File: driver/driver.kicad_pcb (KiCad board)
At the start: 2 copper layers, 131.4 x 100 mm, 99 parts, among them J1 OUT_A, J10 FAN, J2 OUT_B, J4 RJ45_LED_Shielded, J5 RJ45_LED_Shielded, J6 1602 I2C LCD, J7 IN_VCC, J8 IN_GND, J9 SWD, Q1 TPHR6503PL, Q2 TPHR6503PL, Q3 TPHR6503PL, Q4 TPHR6503PL, U1 MT3608, U10 PC817, U11 AMS1117-5.0, U12 PC817, U13 MAX485E, U2 74HC595, U3 AMS1117-3.3, U4 TC4427, U5 TC4427, U6 STM32F030F4Px, U7 INA226, U8 MCP9804_MSOP, U9 PC817, Y1 8MHz

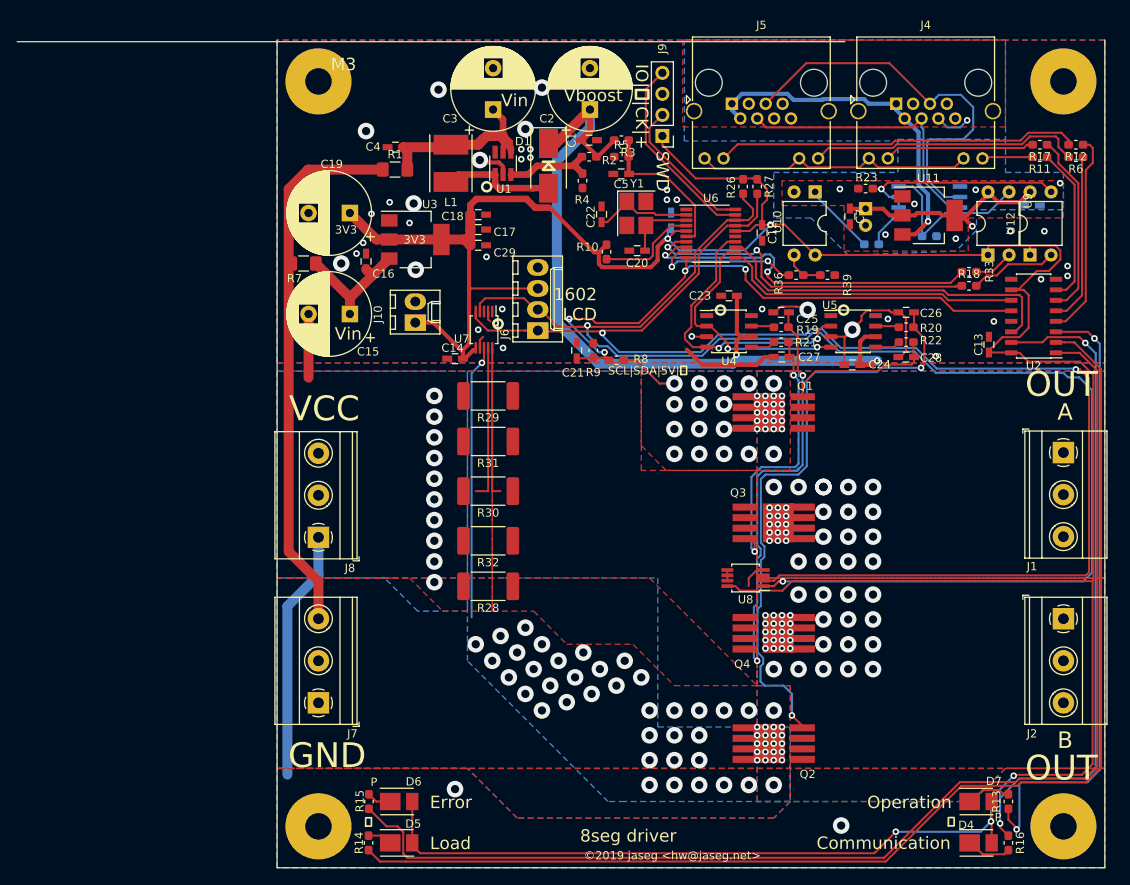
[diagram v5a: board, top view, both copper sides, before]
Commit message: Small adjustments, fix silk
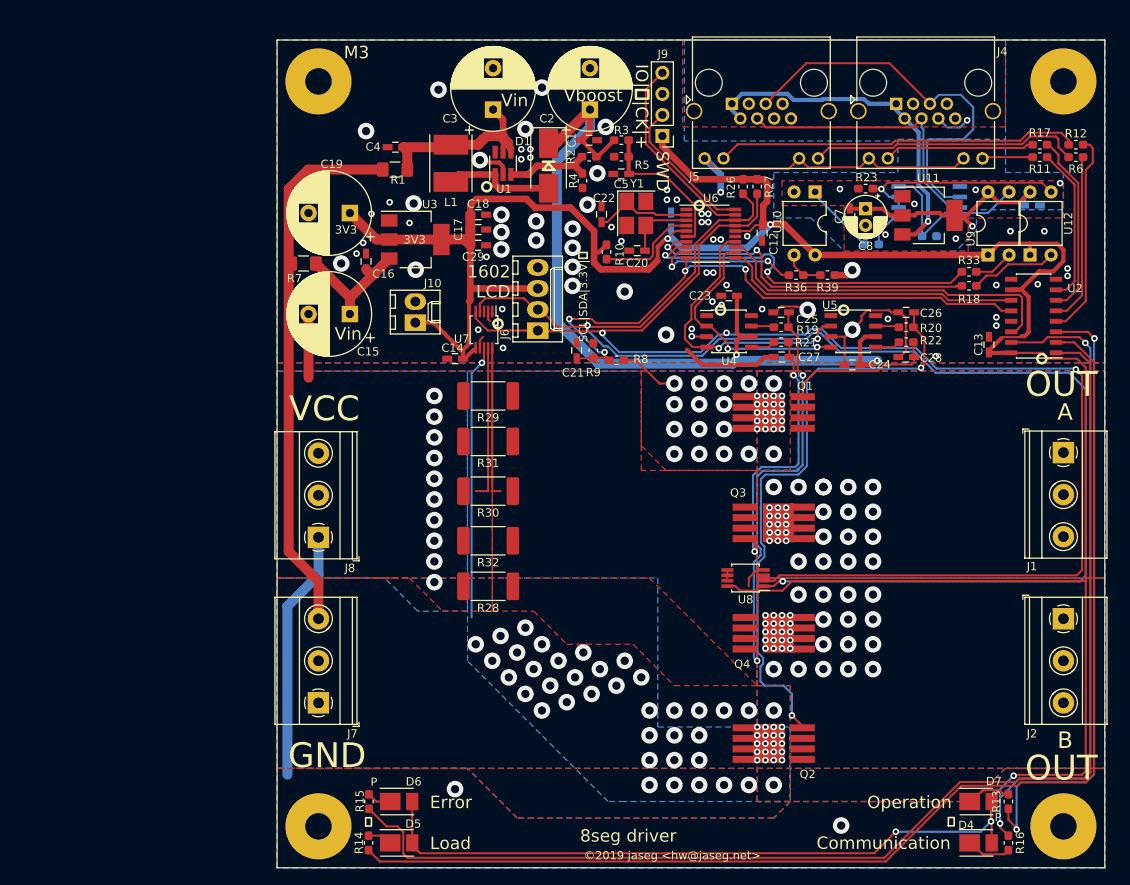
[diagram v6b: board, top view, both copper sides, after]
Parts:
- C8: moved to F.Cu
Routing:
- net +3V3: track 393.5 -> 416.5 mm
- net GND: track 136.6 -> 143.9 mm, vias 49 -> 83
- net /SCL: track 172.4 -> 171.3 mm
- net /SDA: track 176.6 -> 175.6 mm
- net /SLED2: track 148.7 -> 148.0 mm
- net /SLED3: track 150.2 -> 149.5 mm
- net /SLED4: track 79.5 -> 78.8 mm
- net /SLED1: track 76.4 -> 75.7 mm
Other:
- board size 131.4 x 100 mm -> 100 x 100 mm
- board text added: "SCL|SDA|3.3V|⏚"
- board text removed: "SCL|SDA|5V|⏚"

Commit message: driver: Move traces away from board edge
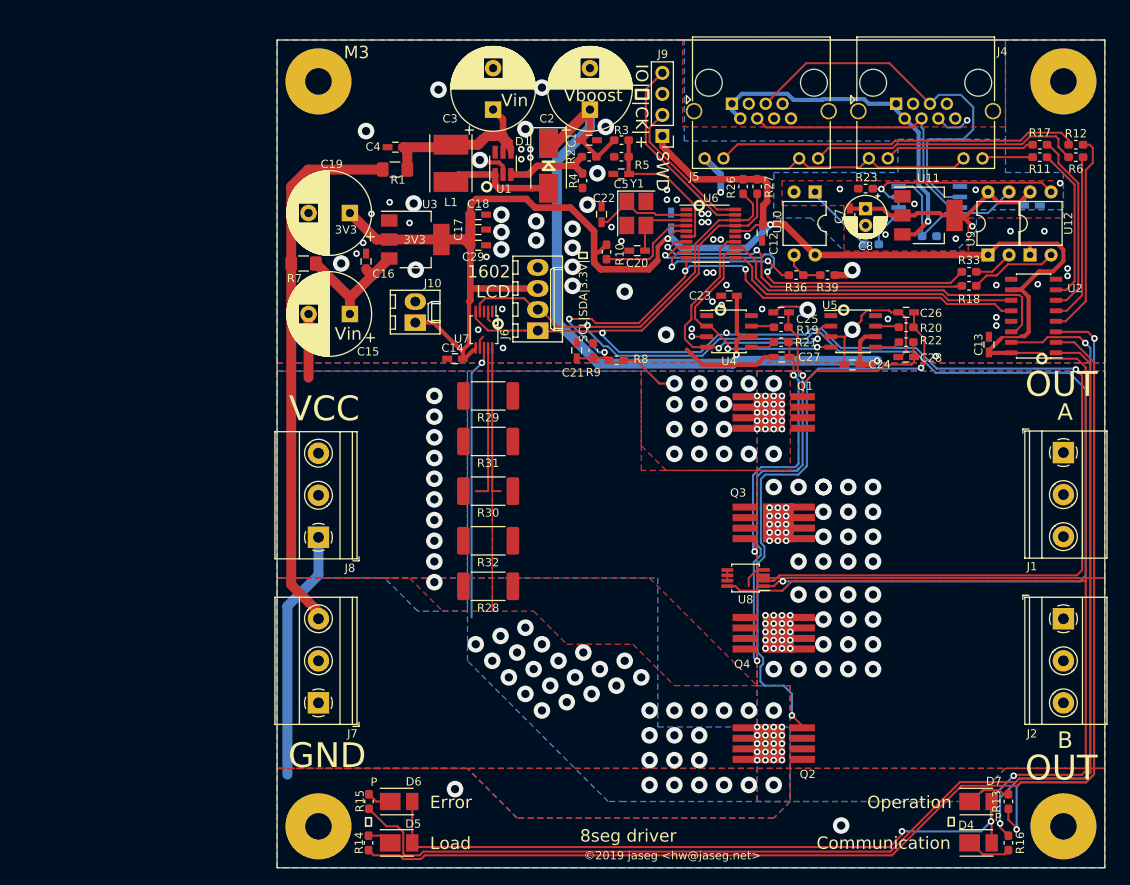
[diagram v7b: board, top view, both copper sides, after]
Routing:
- net +3V3: track 416.5 -> 415.9 mm
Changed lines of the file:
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@@
     (thickness 1.6)
     (drawings 113)
-    (tracks 1098)
+    (tracks 1103)
     (zones 0)
     (modules 99)
@@
       (outputformat 1)
       (mirror false)
-      (drillshape 1)
+      (drillshape 0)
       (scaleselection 1)
-      (outputdirectory ""))
+      (outputdirectory "gerber"))
   )
   (net 0 "")
@@
   (segment (start 93.675 92.5) (end 93.7 92.5) (width 0.5) (layer F.Cu) (net 5))
   (segment (start 86.33 147) (end 86.33 152) (width 0.25) (layer F.Cu) (net 5))
-  (segment (start 86.33 152.3) (end 87.28 153.25) (width 0.25) (layer F.Cu) (net 5))
-  (segment (start 86.33 152) (end 86.33 152.3) (width 0.25) (layer F.Cu) (net 5))
-  (via (at 144.75 150.65) (size 0.8) (drill 0.4) (layers F.Cu B.Cu) (net 5))
-  (segment (start 87.28 153.25) (end 142.15 153.25) (width 0.25) (layer F.Cu) (net 5))
-  (segment (start 142.15 153.25) (end 144.75 150.65) (width 0.25) (layer F.Cu) (net 5))
   (via (at 156.25 149.4) (size 0.8) (drill 0.4) (layers F.Cu B.Cu) (net 5))
-  (segment (start 144.75 150.65) (end 155 150.65) (width 0.25) (layer B.Cu) (net 5))
-  (segment (start 155 150.65) (end 156.25 149.4) (width 0.25) (layer B.Cu) (net 5))
   (segment (start 156.33 149.32) (end 156.25 149.4) (width 0.25) (layer F.Cu) (net 5))
   (segment (start 156.33 147) (end 156.33 149.32) (width 0.25) (layer F.Cu) (net 5))
@@
   (segment (start 163.750001 82.949999) (end 162.050001 82.949999) (width 0.5) (layer F.Cu) (net 5))
   (segment (start 162.050001 82.949999) (end 159.825 85.175) (width 0.5) (layer F.Cu) (net 5))
+  (via (at 145.5 150.6) (size 0.8) (drill 0.4) (layers F.Cu B.Cu) (net 5))
+  (segment (start 155.05 150.6) (end 146.065685 150.6) (width 0.25) (layer B.Cu) (net 5))
+  (segment (start 156.25 149.4) (end 155.05 150.6) (width 0.25) (layer B.Cu) (net 5))
+  (segment (start 146.065685 150.6) (end 145.5 150.6) (width 0.25) (layer B.Cu) (net 5))
+  (segment (start 145.5 151) (end 145.5 150.6) (width 0.25) (layer F.Cu) (net 5))
+  (segment (start 144 152.5) (end 145.5 151) (width 0.25) (layer F.Cu) (net 5))
+  (segment (start 86.33 152) (end 86.83 152.5) (width 0.25) (layer F.Cu) (net 5))
+  (segment (start 86.83 152.5) (end 144 152.5) (width 0.25) (layer F.Cu) (net 5))
   (segment (start 78.8 88.1) (end 78.8 86.15) (width 1.2) (layer F.Cu) (net 6))
   (segment (start 81.5 83.45) (end 80.75 82.7) (width 1.2) (layer F.Cu) (net 6))
@@
   (segment (start 94.75 94) (end 93.5 95.25) (width 0.25) (layer B.Cu) (net 21))
   (segment (start 93.5 95.25) (end 93.5 124.75) (width 0.25) (layer B.Cu) (net 21))
-  (segment (start 73.75 70.65) (end 82.7625 70.65) (width 1.2) (layer F.Cu) (net 21))
-  (segment (start 71.4 73) (end 73.75 70.65) (width 1.2) (layer F.Cu) (net 21))
-  (segment (start 71.4 116.8) (end 71.4 73) (width 1.2) (layer F.Cu) (net 21))
-  (segment (start 75 124.92) (end 75 120.4) (width 1.2) (layer F.Cu) (net 21))
-  (segment (start 75 120.4) (end 71.4 116.8) (width 1.2) (layer F.Cu) (net 21))
   (segment (start 113.4 93.7) (end 111.875 93.7) (width 0.25) (layer F.Cu) (net 21))
   (segment (start 118 96.5) (end 116.2 96.5) (width 0.25) (layer F.Cu) (net 21))
   (segment (start 116.2 96.5) (end 113.4 93.7) (width 0.25) (layer F.Cu) (net 21))
+  (segment (start 73.75 70.65) (end 82.7625 70.65) (width 1.2) (layer F.Cu) (net 21))
+  (segment (start 71.7125 72.6875) (end 73.75 70.65) (width 1.2) (layer F.Cu) (net 21))
+  (segment (start 71.7125 120.8125) (end 71.7125 72.6875) (width 1.2) (layer F.Cu) (net 21))
+  (segment (start 75 124.92) (end 75 124.1) (width 1.2) (layer F.Cu) (net 21))
+  (segment (start 75 124.1) (end 71.7125 120.8125) (width 1.2) (layer F.Cu) (net 21))
   (segment (start 96 92.2) (end 96 109.5) (width 0.25) (layer F.Cu) (net 22))
   (segment (start 96 109.5) (end 97 109.5) (width 0.25) (layer F.Cu) (net 22))
@@
   (segment (start 167.72501 144.67499) (end 159.865374 144.67499) (width 0.25) (layer B.Cu) (net 59))
   (segment (start 159.344239 145.196125) (end 159.344239 149.809325) (width 0.25) (layer B.Cu) (net 59))
-  (segment (start 165.1 91.525) (end 164.1 91.525) (width 0.25) (layer F.Cu) (net 60))
-  (segment (start 168.7 93.91359) (end 166.31141 91.525) (width 0.25) (layer F.Cu) (net 60))
-  (segment (start 167.711421 144.67499) (end 168.7 143.686411) (width 0.25) (layer F.Cu) (net 60))
-  (segment (start 159.865374 144.67499) (end 167.711421 144.67499) (width 0.25) (layer F.Cu) (net 60))
-  (segment (start 143.5364 154.250011) (end 152.6864 145.100011) (width 0.25) (layer F.Cu) (net 60))
-  (segment (start 82.42501 154.25001) (end 85.558598 154.250011) (width 0.25) (layer F.Cu) (net 60))
-  (segment (start 152.6864 145.100011) (end 159.440353 145.100011) (width 0.25) (layer F.Cu) (net 60))
-  (segment (start 81.05 152.875) (end 82.42501 154.25001) (width 0.25) (layer F.Cu) (net 60))
-  (segment (start 85.558598 154.250011) (end 143.5364 154.250011) (width 0.25) (layer F.Cu) (net 60))
-  (segment (start 166.31141 91.525) (end 165.1 91.525) (width 0.25) (layer F.Cu) (net 60))
-  (segment (start 159.440353 145.100011) (end 159.865374 144.67499) (width 0.25) (layer F.Cu) (net 60))
-  (segment (start 168.7 143.686411) (end 168.7 93.91359) (width 0.25) (layer F.Cu) (net 60))
-  (segment (start 168.249989 94.099989) (end 168.249989 143.500011) (width 0.25) (layer F.Cu) (net 61))
-  (segment (start 164.1 92.795) (end 166.945 92.795) (width 0.25) (layer F.Cu) (net 61))
-  (segment (start 83.225 150) (end 81.599072 148.374072) (width 0.25) (layer F.Cu) (net 61))
-  (segment (start 143.35 153.8) (end 85.744998 153.8) (width 0.25) (layer F.Cu) (net 61))
+  (segment (start 84.8 153.5) (end 81.675 153.5) (width 0.25) (layer F.Cu) (net 60))
+  (segment (start 85.250011 153.950011) (end 84.8 153.5) (width 0.25) (layer F.Cu) (net 60))
+  (segment (start 144.286411 153.5) (end 87.851413 153.5) (width 0.25) (layer F.Cu) (net 60))
+  (segment (start 152.6864 145.100011) (end 144.286411 153.5) (width 0.25) (layer F.Cu) (net 60))
+  (segment (start 159.440353 145.100011) (end 152.6864 145.100011) (width 0.25) (layer F.Cu) (net 60))
+  (segment (start 166.31141 91.525) (end 168.7 93.913589) (width 0.25) (layer F.Cu) (net 60))
+  (segment (start 168.7 93.913589) (end 168.7 143.686411) (width 0.25) (layer F.Cu) (net 60))
+  (segment (start 164.1 91.525) (end 166.31141 91.525) (width 0.25) (layer F.Cu) (net 60))
+  (segment (start 81.675 153.5) (end 81.05 152.875) (width 0.25) (layer F.Cu) (net 60))
+  (segment (start 159.865374 144.67499) (end 159.440353 145.100011) (width 0.25) (layer F.Cu) (net 60))
+  (segment (start 87.401402 153.950011) (end 85.250011 153.950011) (width 0.25) (layer F.Cu) (net 60))
+  (segment (start 87.851413 153.5) (end 87.401402 153.950011) (width 0.25) (layer F.Cu) (net 60))
+  (segment (start 168.7 143.686411) (end 167.711421 144.67499) (width 0.25) (layer F.Cu) (net 60))
+  (segment (start 167.711421 144.67499) (end 159.865374 144.67499) (width 0.25) (layer F.Cu) (net 60))
   (segment (start 81.599072 148.374072) (end 81.1 147.875) (width 0.25) (layer F.Cu) (net 61))
-  (segment (start 85.744998 153.8) (end 85.245001 153.300003) (width 0.25) (layer F.Cu) (net 61))
-  (segment (start 85.245001 153.300003) (end 85.245001 150.689999) (width 0.25) (layer F.Cu) (net 61))
-  (segment (start 166.945 92.795) (end 168.249989 94.099989) (width 0.25) (layer F.Cu) (net 61))
+  (segment (start 83.225 150) (end 81.599072 148.374072) (width 0.25) (layer F.Cu) (net 61))
   (segment (start 85.245001 150.689999) (end 84.555002 150) (width 0.25) (layer F.Cu) (net 61))
+  (segment (start 87.215002 153.5) (end 85.444998 153.5) (width 0.25) (layer F.Cu) (net 61))
   (segment (start 159.253953 144.65) (end 152.5 144.65) (width 0.25) (layer F.Cu) (net 61))
   (segment (start 84.555002 150) (end 83.225 150) (width 0.25) (layer F.Cu) (net 61))
-  (segment (start 152.5 144.65) (end 143.35 153.8) (width 0.25) (layer F.Cu) (net 61))
-  (segment (start 159.678974 144.224979) (end 159.253953 144.65) (width 0.25) (layer F.Cu) (net 61))
   (segment (start 167.525021 144.224979) (end 159.678974 144.224979) (width 0.25) (layer F.Cu) (net 61))
   (segment (start 168.249989 143.500011) (end 167.525021 144.224979) (width 0.25) (layer F.Cu) (net 61))
+  (segment (start 85.245001 153.300003) (end 85.245001 150.689999) (width 0.25) (layer F.Cu) (net 61))
+  (segment (start 144.100011 153.049989) (end 87.665013 153.049989) (width 0.25) (layer F.Cu) (net 61))
+  (segment (start 164.1 92.795) (end 166.945 92.795) (width 0.25) (layer F.Cu) (net 61))
+  (segment (start 152.5 144.65) (end 144.100011 153.049989) (width 0.25) (layer F.Cu) (net 61))
+  (segment (start 87.665013 153.049989) (end 87.215002 153.5) (width 0.25) (layer F.Cu) (net 61))
+  (segment (start 85.444998 153.5) (end 85.245001 153.300003) (width 0.25) (layer F.Cu) (net 61))
+  (segment (start 159.678974 144.224979) (end 159.253953 144.65) (width 0.25) (layer F.Cu) (net 61))
+  (segment (start 166.945 92.795) (end 168.249989 94.099989) (width 0.25) (layer F.Cu) (net 61))
+  (segment (start 168.249989 94.099989) (end 168.249989 143.500011) (width 0.25) (layer F.Cu) (net 61))
   (via (at 167.65 91.6) (size 0.8) (drill 0.4) (layers F.Cu B.Cu) (net 62))
   (segment (start 166.949999 90.899999) (end 167.65 91.6) (width 0.25) (layer F.Cu) (net 62))

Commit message: driver: Add mounting holes for heatsink
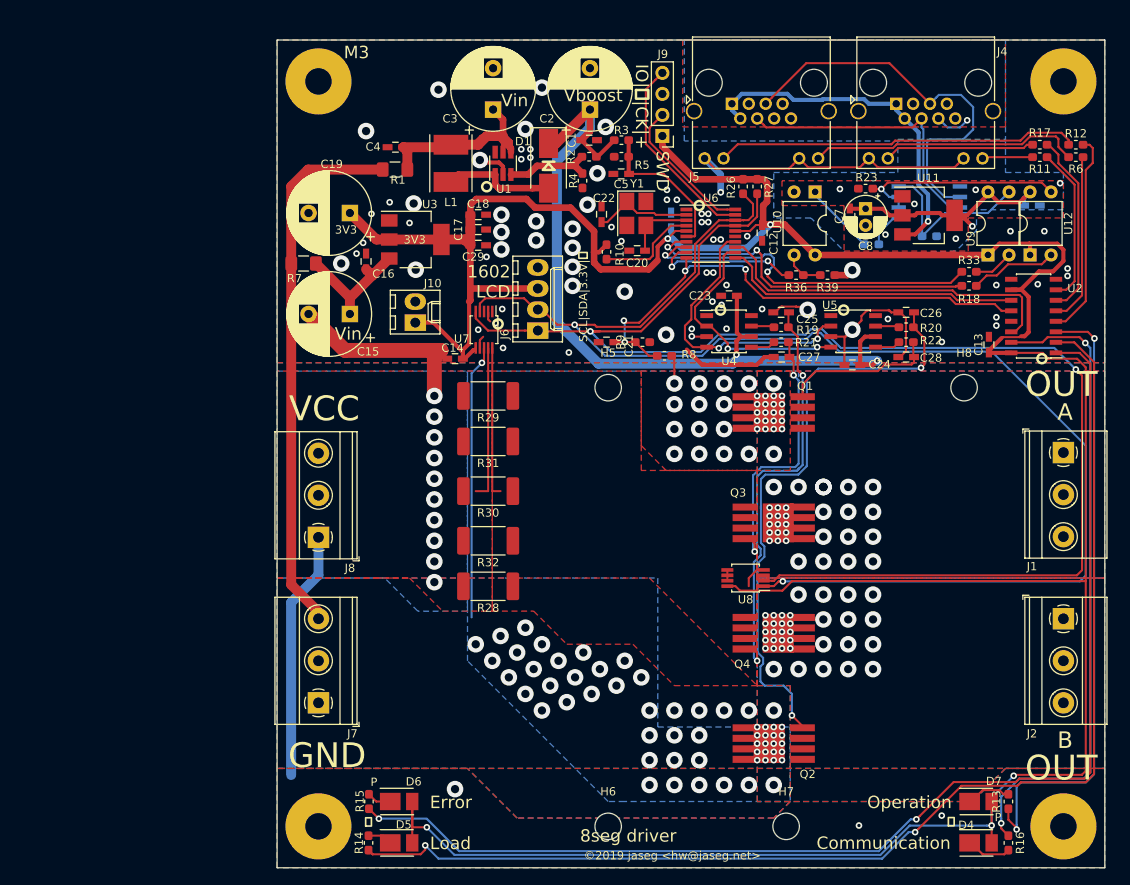
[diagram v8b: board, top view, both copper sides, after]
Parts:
- added H5: MountingHole, MountingHole:MountingHole_3.2mm_M3, F.Cu at (110.0, 97.0)
- added H6: MountingHole, MountingHole:MountingHole_3.2mm_M3, F.Cu at (110.0, 150.0)
- added H7: MountingHole, MountingHole:MountingHole_3.2mm_M3, F.Cu at (131.5, 150.0)
- added H8: MountingHole, MountingHole:MountingHole_3.2mm_M3, F.Cu at (153.0, 97.0)
- moved R9 6.03 mm to (114.2, 91.5), turned to 180 degrees
- moved R8 5.83 mm to (116.8, 93.2)
- moved C21 3.74 mm to (109.8, 91.5), turned to 180 degrees
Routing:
- net GND: track 143.9 -> 159.7 mm, vias 83 -> 85
- net /VIN_MON: track 73.0 -> 63.3 mm
- net +3V3: track 415.9 -> 420.7 mm
- net /VIN: track 105.9 -> 102.1 mm
- net /SDA: track 175.6 -> 172.1 mm
- net /SCL: track 171.3 -> 173.5 mm
- net /SLED3: track 149.2 -> 147.3 mm, vias 0 -> 2
- net /SLED2: track 147.7 -> 148.9 mm, vias 0 -> 2
